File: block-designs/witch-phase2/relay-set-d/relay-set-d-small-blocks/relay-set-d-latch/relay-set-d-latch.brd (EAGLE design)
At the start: 98.8 x 51.6 mm, 55 parts, among them IC1 74LVC1G125DBV, IC10 741G175, IC11 74LVC1G06DBV, IC12 74LVC1G06DBV, IC13 74LVC1G06DBV, IC14 74LVC1G06DBV, IC15 74LVC1G06DBV, IC16 74LVC1G14DBV, IC2 74LVC1G125DBV, IC3 74LVC1G125DBV, IC4 74LVC1G125DBV, IC5 74LVC1G125DBV, IC6 741G175, IC7 741G175, IC8 741G175, IC9 741G175, Q1 MMBT2907ALT1SMD, Q2 MMBT2907ALT1SMD

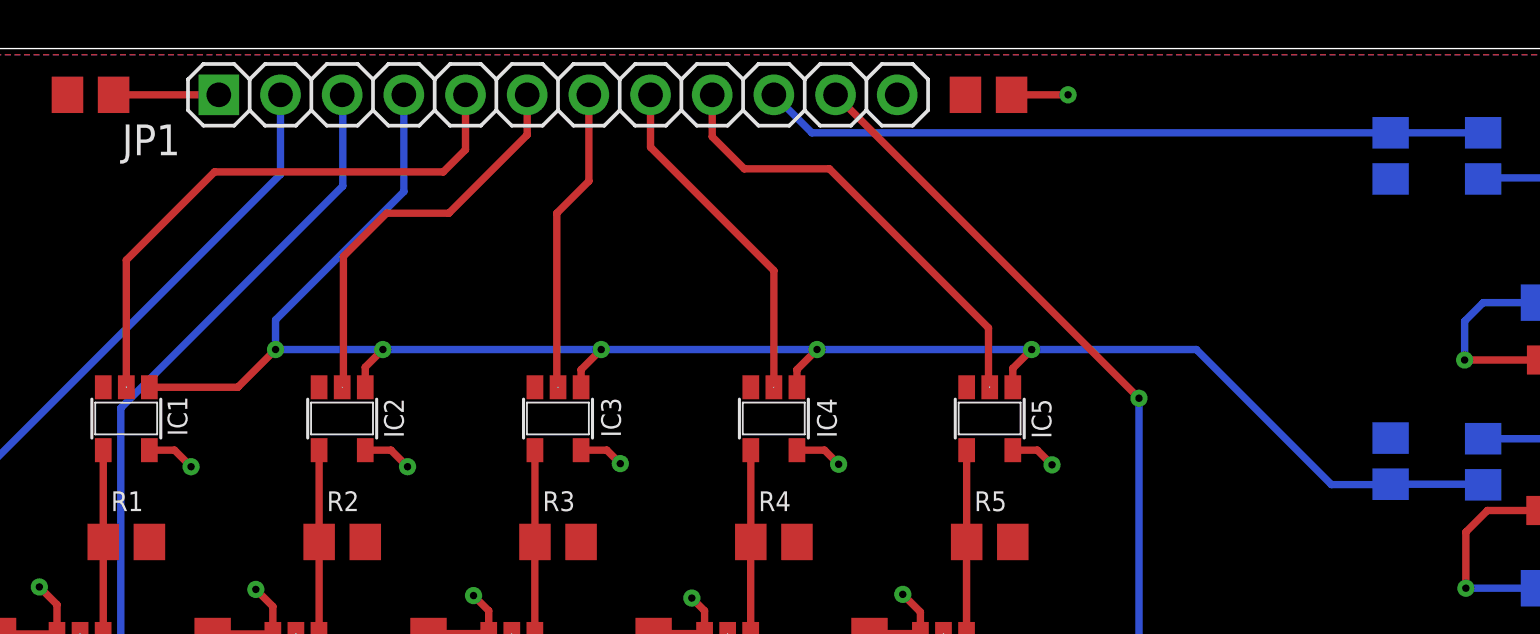
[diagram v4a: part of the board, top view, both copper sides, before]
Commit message: add inverting schemitt trigger for enable line and connect valdata led
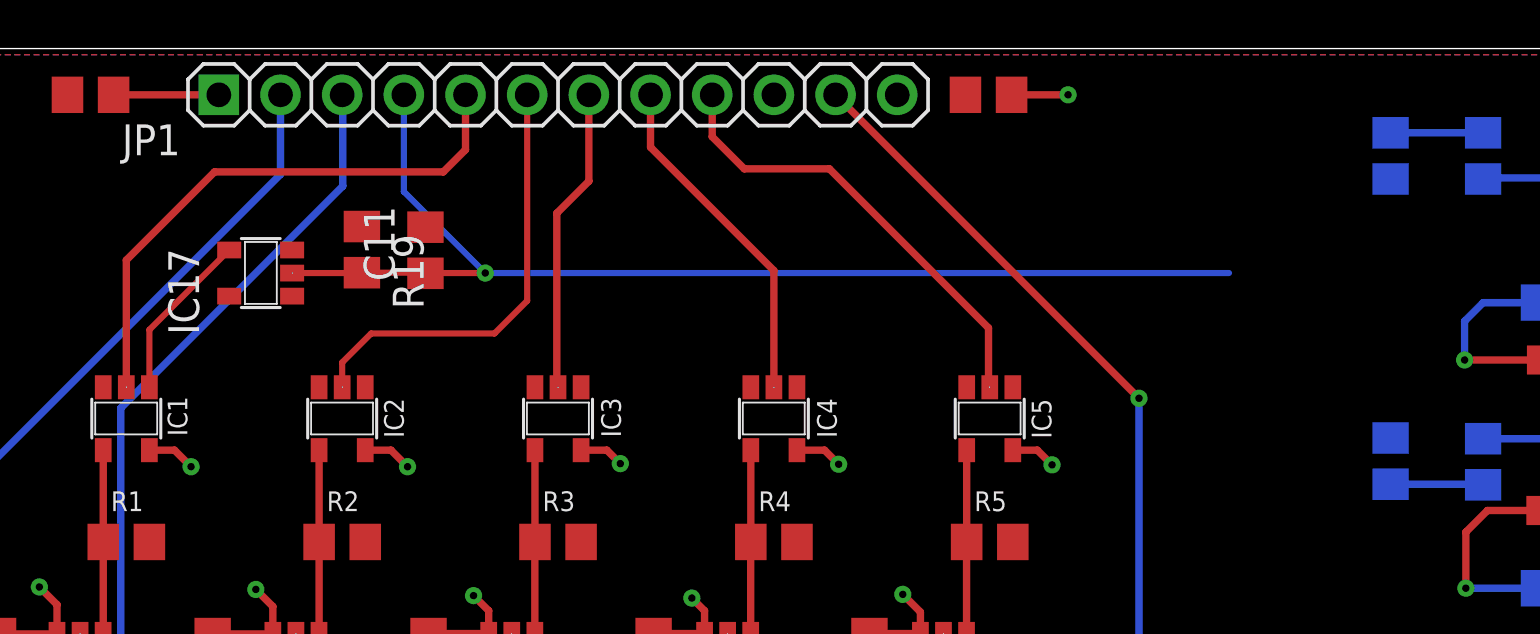
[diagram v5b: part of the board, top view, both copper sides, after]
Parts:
- added C11: 1uF, resistor:C0805
- added IC17: 74LVC1G14DBV, 74xx-little-us:SOT23-5
- added R19: (no value), resistor:R0805
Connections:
- removed net DATA_N: C10.1, IC11.4, IC12.4, IC13.4, IC14.4, IC15.4, IC16.2, R11.2
- removed net DM: JP1.10, R12.2, R14.2
- new net !DATA: C10.1, IC11.4, IC12.4, IC13.4, IC14.4, IC15.4, IC16.2, R11.2, R12.2, R14.2
- new net !ENABLE: IC1.1, IC17.4, IC2.1, IC3.1, IC4.1, IC5.1
- net DGA: now also C11.1, IC17.2, R19.2; no longer IC1.1, IC2.1, IC3.1, IC4.1, IC5.1
- net GND: now also C11.2, IC17.3
- net VCC: now also IC17.5, R19.1
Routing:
- net !DATA: track 0.00 -> 66.9 mm
- net DATA_N: track 62.9 -> 0.00 mm
- net DM: track 30.1 -> 0.00 mm
- net DGA: track 78.1 -> 51.2 mm, vias 5 -> 1
- net !ENABLE: track 0.00 -> 7.02 mm
- net DB_IN: track 16.7 -> 18.2 mm
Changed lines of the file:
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@@
 <attribute name="VALUE" x="21.5138" y="12.1158" size="1.27" layer="27" rot="R90"/>
 </element>
+<element name="R19" library="resistor" package="R0805" value="" x="41.4528" y="43.2816" rot="R270"/>
+<element name="C11" library="resistor" package="C0805" value="1uF" x="44.069" y="43.2562" rot="R90"/>
+<element name="IC17" library="74xx-little-us" package="SOT23-5" value="74LVC1G14DBV" x="37.2872" y="42.3164" rot="R90"/>
 </elements>
 <signals>
@@
 <contactref element="IC16" pad="3"/>
 <contactref element="C10" pad="2"/>
+<contactref element="IC17" pad="3"/>
+<contactref element="C11" pad="2"/>
 </signal>
 <signal name="DA">
@@
 <contactref element="R15" pad="2"/>
 <contactref element="R13" pad="2"/>
-<contactref element="IC1" pad="1"/>
-<contactref element="IC2" pad="1"/>
-<contactref element="IC3" pad="1"/>
-<contactref element="IC4" pad="1"/>
-<contactref element="IC5" pad="1"/>
 <wire x1="83.82" y1="33.6194" x2="87.6046" y2="33.6194" width="0.3048" layer="16"/>
 <wire x1="87.6046" y1="33.6194" x2="87.63" y2="33.594" width="0.3048" layer="16"/>
-<wire x1="32.7" y1="37.612" x2="36.342" y2="37.612" width="0.3048" layer="1"/>
-<wire x1="36.342" y1="37.612" x2="37.8968" y2="39.1668" width="0.3048" layer="1"/>
-<via x="37.8968" y="39.1668" extent="1-16" drill="0.3048"/>
-<wire x1="37.8968" y1="39.1668" x2="42.3164" y2="39.1668" width="0.3048" layer="16"/>
-<wire x1="42.3164" y1="39.1668" x2="51.308" y2="39.1668" width="0.3048" layer="16"/>
-<wire x1="51.308" y1="39.1668" x2="60.198" y2="39.1668" width="0.3048" layer="16"/>
-<wire x1="60.198" y1="39.1668" x2="69.0372" y2="39.1668" width="0.3048" layer="16"/>
-<wire x1="69.0372" y1="39.1668" x2="75.819" y2="39.1668" width="0.3048" layer="16"/>
-<wire x1="75.819" y1="39.1668" x2="81.3816" y2="33.6042" width="0.3048" layer="16"/>
-<wire x1="81.3816" y1="33.6042" x2="83.8048" y2="33.6042" width="0.3048" layer="16"/>
 <wire x1="83.8048" y1="33.6042" x2="83.82" y2="33.6194" width="0.3048" layer="16"/>
-<wire x1="41.59" y1="37.612" x2="41.59" y2="38.4404" width="0.3048" layer="1"/>
-<wire x1="41.59" y1="38.4404" x2="42.3164" y2="39.1668" width="0.3048" layer="1"/>
-<via x="42.3164" y="39.1668" extent="1-16" drill="0.3048"/>
-<wire x1="50.48" y1="37.612" x2="50.48" y2="38.3388" width="0.3048" layer="1"/>
-<wire x1="50.48" y1="38.3388" x2="51.308" y2="39.1668" width="0.3048" layer="1"/>
-<via x="51.308" y="39.1668" extent="1-16" drill="0.3048"/>
-<wire x1="59.37" y1="37.612" x2="59.37" y2="38.3388" width="0.3048" layer="1"/>
-<wire x1="59.37" y1="38.3388" x2="60.198" y2="39.1668" width="0.3048" layer="1"/>
-<via x="60.198" y="39.1668" extent="1-16" drill="0.3048"/>
-<wire x1="68.26" y1="37.612" x2="68.26" y2="38.3896" width="0.3048" layer="1"/>
-<wire x1="68.26" y1="38.3896" x2="69.0372" y2="39.1668" width="0.3048" layer="1"/>
-<via x="69.0372" y="39.1668" extent="1-16" drill="0.3048"/>
 <contactref element="JP1" pad="4"/>
-<wire x1="37.8968" y1="39.1668" x2="37.8968" y2="40.386" width="0.3048" layer="16"/>
-<wire x1="37.8968" y1="40.386" x2="43.18" y2="45.6692" width="0.3048" layer="16"/>
-<wire x1="43.18" y1="45.6692" x2="43.18" y2="49.657" width="0.3048" layer="16"/>
+<contactref element="R19" pad="2"/>
+<contactref element="C11" pad="1"/>
+<contactref element="IC17" pad="2"/>
+<wire x1="38.5772" y1="42.3164" x2="41.4376" y2="42.3164" width="0.254" layer="1"/>
+<wire x1="41.4376" y1="42.3164" x2="41.4528" y2="42.3316" width="0.254" layer="1"/>
+<wire x1="41.4528" y1="42.3316" x2="44.0436" y2="42.3316" width="0.254" layer="1"/>
+<wire x1="44.0436" y1="42.3316" x2="44.069" y2="42.3062" width="0.254" layer="1"/>
+<wire x1="43.18" y1="49.657" x2="43.18" y2="45.6692" width="0.254" layer="16"/>
+<wire x1="43.18" y1="45.6692" x2="46.5328" y2="42.3164" width="0.254" layer="16"/>
+<via x="46.5328" y="42.3164" extent="1-16" drill="0.3048"/>
+<wire x1="46.5328" y1="42.3164" x2="44.0792" y2="42.3164" width="0.254" layer="1"/>
+<wire x1="44.0792" y1="42.3164" x2="44.069" y2="42.3062" width="0.254" layer="1"/>
+<wire x1="46.5328" y1="42.3164" x2="77.1652" y2="42.3164" width="0.254" layer="16"/>
+<wire x1="77.1652" y1="42.3164" x2="83.82" y2="33.6194" width="0" layer="19" extent="16-16"/>
 </signal>
 <signal name="RESET">
@@
 <wire x1="16.4338" y1="13.6758" x2="16.4338" y2="11.811" width="0.3048" layer="1"/>
 <via x="16.4338" y="11.811" extent="1-16" drill="0.3048"/>
+<contactref element="IC17" pad="5"/>
+<contactref element="R19" pad="1"/>
+<wire x1="35.9872" y1="41.3664" x2="41.4528" y2="44.2316" width="0" layer="19" extent="1-1"/>
+<wire x1="33.7358" y1="35.022" x2="35.9872" y2="41.3664" width="0" layer="19" extent="1-1"/>
 </signal>
 <signal name="DSA-DSB">
@@
 <contactref element="IC2" pad="2"/>
 <contactref element="JP1" pad="6"/>
-<wire x1="48.26" y1="49.657" x2="48.26" y2="48.006" width="0.3048" layer="1"/>
-<wire x1="48.26" y1="48.006" x2="45.0342" y2="44.7802" width="0.3048" layer="1"/>
-<wire x1="45.0342" y1="44.7802" x2="42.4688" y2="44.7802" width="0.3048" layer="1"/>
-<wire x1="42.4688" y1="44.7802" x2="40.6908" y2="43.0022" width="0.3048" layer="1"/>
-<wire x1="40.6908" y1="43.0022" x2="40.6908" y2="37.6628" width="0.3048" layer="1"/>
-<wire x1="40.6908" y1="37.6628" x2="40.64" y2="37.612" width="0.3048" layer="1"/>
+<wire x1="48.26" y1="49.657" x2="48.26" y2="41.1734" width="0.254" layer="1"/>
+<wire x1="48.26" y1="41.1734" x2="46.9138" y2="39.8272" width="0.254" layer="1"/>
+<wire x1="46.9138" y1="39.8272" x2="41.8338" y2="39.8272" width="0.254" layer="1"/>
+<wire x1="41.8338" y1="39.8272" x2="40.64" y2="38.6334" width="0.254" layer="1"/>
+<wire x1="40.64" y1="38.6334" x2="40.64" y2="37.612" width="0.254" layer="1"/>
 </signal>
 <signal name="DC_IN">
@@
 <wire x1="87.63" y1="41.0972" x2="89.8296" y2="41.0972" width="0.3048" layer="16"/>
 </signal>
-<signal name="DM">
+<signal name="!DATA">
 <contactref element="R14" pad="2"/>
 <contactref element="R12" pad="2"/>
 <wire x1="87.6046" y1="48.3464" x2="87.63" y2="48.0924" width="0.3048" layer="16"/>
-<contactref element="JP1" pad="10"/>
-<wire x1="58.42" y1="49.657" x2="59.9846" y2="48.0924" width="0.3048" layer="16"/>
 <wire x1="83.82" y1="48.0924" x2="87.63" y2="48.0924" width="0.3048" layer="16"/>
-<wire x1="59.9846" y1="48.0924" x2="83.82" y2="48.0924" width="0.3048" layer="16"/>
-</signal>
-<signal name="DATA_N">
 <contactref element="IC15" pad="4"/>
 <contactref element="IC11" pad="4"/>
@@
 <wire x1="18.9938" y1="14.6456" x2="18.9938" y2="14.6558" width="0.3048" layer="1"/>
 <wire x1="23.749" y1="14.6456" x2="23.749" y2="11.9228" width="0.3048" layer="1"/>
+<wire x1="63.5152" y1="14.702" x2="83.82" y2="48.0924" width="0" layer="19" extent="1-16"/>
 </signal>
 <signal name="N$20">
@@
 <wire x1="38.1" y1="46.3804" x2="38.1" y2="49.657" width="0.3048" layer="16"/>
 </signal>
+<signal name="!ENABLE">
+<contactref element="IC1" pad="1"/>
+<contactref element="IC2" pad="1"/>
+<contactref element="IC3" pad="1"/>
+<contactref element="IC4" pad="1"/>
+<contactref element="IC5" pad="1"/>
+<contactref element="IC17" pad="4"/>
+<wire x1="35.9872" y1="43.2664" x2="32.7" y2="39.9792" width="0.254" layer="1"/>
+<wire x1="32.7" y1="39.9792" x2="32.7" y2="37.612" width="0.254" layer="1"/>
+<wire x1="59.37" y1="37.612" x2="68.26" y2="37.612" width="0" layer="19" extent="1-1"/>
+<wire x1="50.48" y1="37.612" x2="59.37" y2="37.612" width="0" layer="19" extent="1-1"/>
+<wire x1="41.59" y1="37.612" x2="50.48" y2="37.612" width="0" layer="19" extent="1-1"/>
+<wire x1="35.9872" y1="43.2664" x2="41.59" y2="37.612" width="0" layer="19" extent="1-1"/>
+</signal>
 </signals>

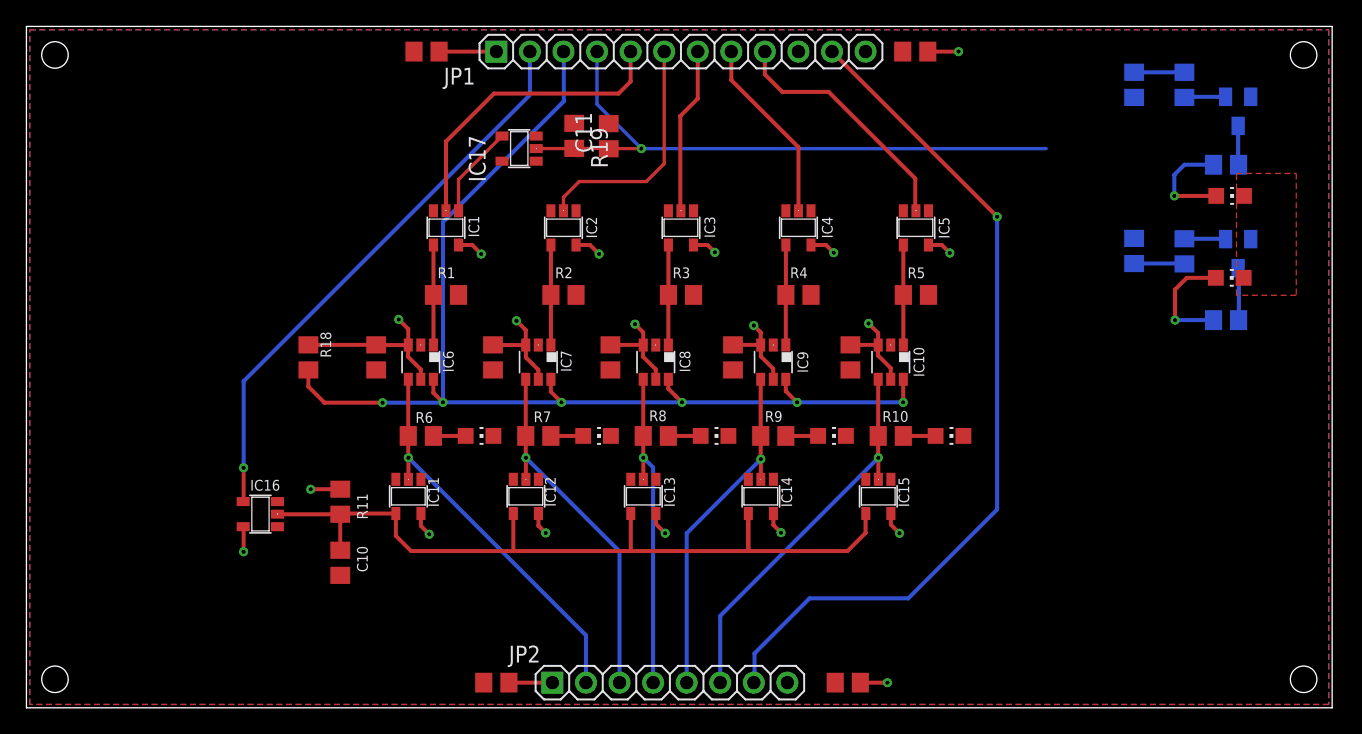
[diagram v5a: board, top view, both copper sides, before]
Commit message: updated layout for easier interfacing
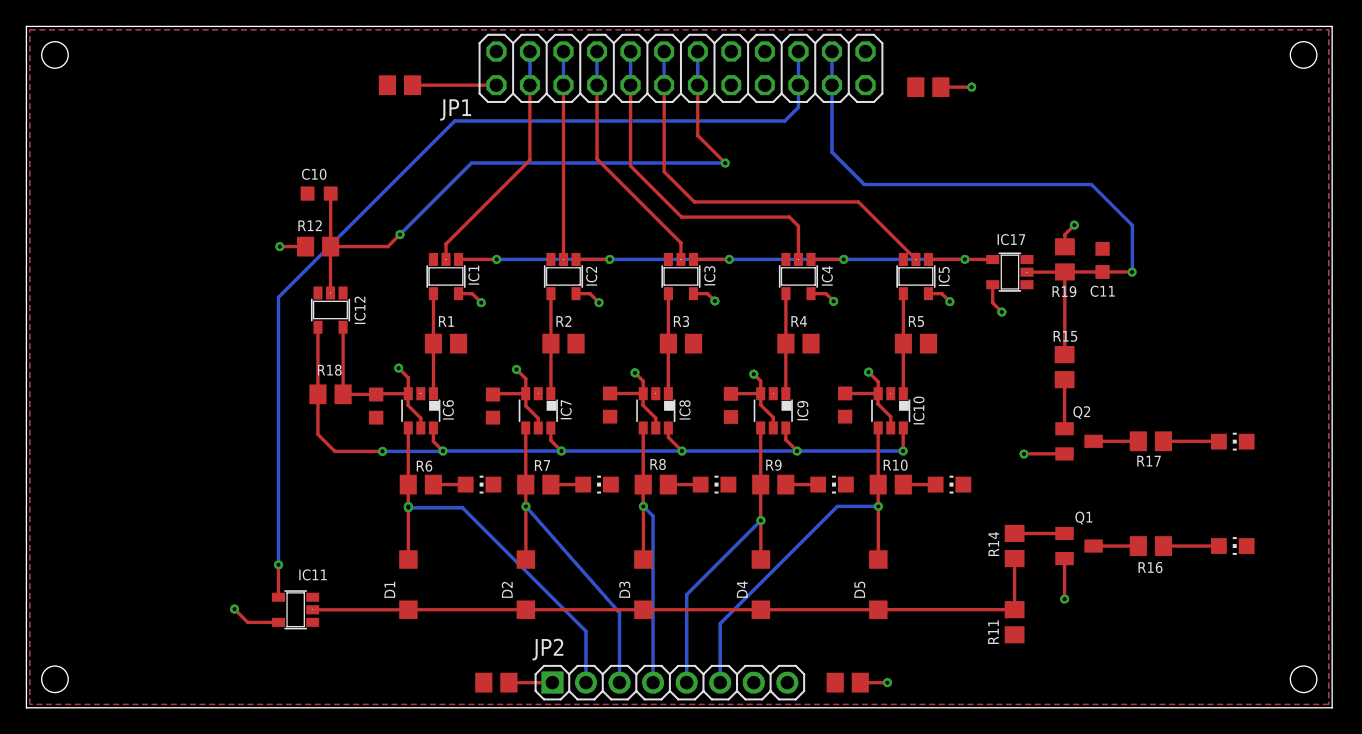
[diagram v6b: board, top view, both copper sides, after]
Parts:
- removed IC13, IC14, IC15: 74LVC1G06DBV, 74xx-little-us:SOT23-5
- removed IC16: 74LVC1G14DBV, 74xx-little-us:SOT23-5
- removed R13: (no value), resistor:R0805
- added D1, D2, D3, D4, D5: MBR0520LT, diode:SOD123
- C10, C11, C5, C6, C7, C8, C9: device resistor:C0805 -> resistor:C0603K
- IC11, IC12: value 74LVC1G06DBV -> 74LVC1G17DBV
- JP1: device pinhead:1X12 -> custom-pinhead:2X12
- moved R12 62.9 mm to (22.1, 34.9), flipped to the top, turned to 0 degrees
- moved R11 51.8 mm to (74.8, 6.48)
- moved C11 38.5 mm to (81.4, 33.9)
- moved IC17 38.3 mm to (74.4, 33.0)
- moved R19 38.3 mm to (78.6, 33.9)
- moved R14 37.2 mm to (74.8, 12.2), flipped to the top, turned to 270 degrees
- moved Q1 35.0 mm to (79.7, 12.2), flipped to the top, turned to 270 degrees
- moved R16 29.4 mm to (85.1, 12.2), flipped to the top
- moved C10 28.0 mm to (22.1, 38.9), turned to 180 degrees
- moved LED6 26.5 mm to (91.3, 12.2)
- moved IC12 20.4 mm to (23.0, 30.1)
- moved Q2 18.6 mm to (79.7, 20.2), flipped to the top, turned to 270 degrees
- moved R15 12.6 mm to (78.6, 25.8), flipped to the top, turned to 90 degrees
- moved LED7 12.4 mm to (91.3, 20.1)
- moved IC11 12.1 mm to (20.4, 7.42), turned to 90 degrees
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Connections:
- removed net !DATA: C10.1, IC11.4, IC12.4, IC13.4, IC14.4, IC15.4, IC16.2, R11.2, R12.2, R14.2
- removed net DGA: C11.1, IC17.2, JP1.4, R13.2, R15.2, R19.2
- removed net DSA-DSB: JP1.11, JP2.7
- removed net RESET: IC10.6, IC6.6, IC7.6, IC8.6, IC9.6, JP1.3, R18.1
- new net !CLEAR: IC10.6, IC12.4, IC6.6, IC7.6, IC8.6, IC9.6, R18.1
- new net !RESET: C10.1, IC12.2, JP1.13, JP1.14, R12.2
- new net DATA: D1.C, D2.C, D3.C, D4.C, D5.C, IC11.2, R11.1, R14.2
- new net SELECT: C11.1, IC17.2, JP1.21, JP1.22, R15.2, R19.2
- net DA_IN: now also JP1.3, JP1.4; no longer JP1.5
- net DA_OUT: now also D1.A; no longer IC11.2
- net DB_IN: now also JP1.5
- net DB_OUT: now also D2.A; no longer IC12.2
- net DC_IN: now also JP1.8
- net DC_OUT: now also D3.A; no longer IC13.2
- net DD_IN: now also JP1.10, JP1.9; no longer JP1.8
- net DD_OUT: now also D4.A; no longer IC14.2
- net DE_IN: now also JP1.11, JP1.12; no longer JP1.9
- net DE_OUT: now also D5.A; no longer IC15.2
- net GND: now also JP1.15, JP1.16, JP1.23, JP1.24, R11.2; no longer IC13.3, IC14.3, IC15.3, IC16.3, JP1.12
- net VALDATA: now also IC11.4, JP1.19, JP1.20; no longer IC16.4, JP1.2
- net VCC: now also JP1.17, JP1.18, JP1.2; no longer IC13.5, IC14.5, IC15.5, IC16.5, R11.1, R13.1
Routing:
- net RESET: track 87.3 -> 0.00 mm, vias 6 -> 0
- net !DATA: track 66.9 -> 0.00 mm
- net DSA-DSB: track 64.9 -> 0.00 mm, vias 1 -> 0
- net !CLEAR: track 0.00 -> 63.1 mm, vias 0 -> 6
- net DATA: track 0.00 -> 57.0 mm
- net DGA: track 51.2 -> 0.00 mm, vias 1 -> 0
- net SELECT: track 0.00 -> 50.4 mm, vias 0 -> 1
- net !RESET: track 0.00 -> 49.3 mm, vias 0 -> 2
- net !ENABLE: track 7.02 -> 51.0 mm, vias 0 -> 5
- net VALDATA: track 43.1 -> 72.2 mm
- net DE_IN: track 18.8 -> 30.9 mm
- net DD_IN: track 14.1 -> 25.8 mm
- net VCC: track 76.1 -> 84.5 mm, vias 19 -> 18
- net DC_IN: track 12.6 -> 18.4 mm
- net DA_IN: track 23.4 -> 18.4 mm
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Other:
- board text added: "SEL"
- board text added: "VAL"
- board text removed: "INPUT"
- board text removed: "OUTPUT"
